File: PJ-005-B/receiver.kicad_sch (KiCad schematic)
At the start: 0 parts

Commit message: -- Transmitter with pre-amp LM7171 and power amp LT1210 -- Receiver with charge amp-->inverting amp-->4th order filter-->Inverting amp-->buffer -- Power with LDO 12V to 9V, 9V to 6V, 6V to 5V, 5V to 2.5V and -5V to -2.5V
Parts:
- added J3: Conn_01x02_Pin, symbol Connector:Conn_01x02_Pin
- added R50: 0R, symbol Device:R
- added U14: MD0105K6-G, symbol Echosounder Transceiver:MD0105K6-G
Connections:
- new net: J3.2 (Pin_2), U14.2 (A1)
- new net Charge Amp + Inverting Amp/AMP_OUT: R50.1
- new net Charge Amp + Inverting Amp/CHARGE_AMP_IN: U14.17 (B1)
- new net Filter + Inverting Amp + Buffer/FILTER_IN: R50.2
- new net GND: J3.1 (Pin_1), U14.19 (EPAD)
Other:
- added sheet Charge Amp + Inverting Amp (charge amp & inverting amp.kicad_sch)
- added sheet Filter + Inverting Amp + Buffer (filter & inverting amp & buffer.kicad_sch)
- added sheet PGA (pga.kicad_sch)
- company: (none) -> Xalten Systems Pvt. Ltd.
- title: (none) -> Echosounder Transceiver

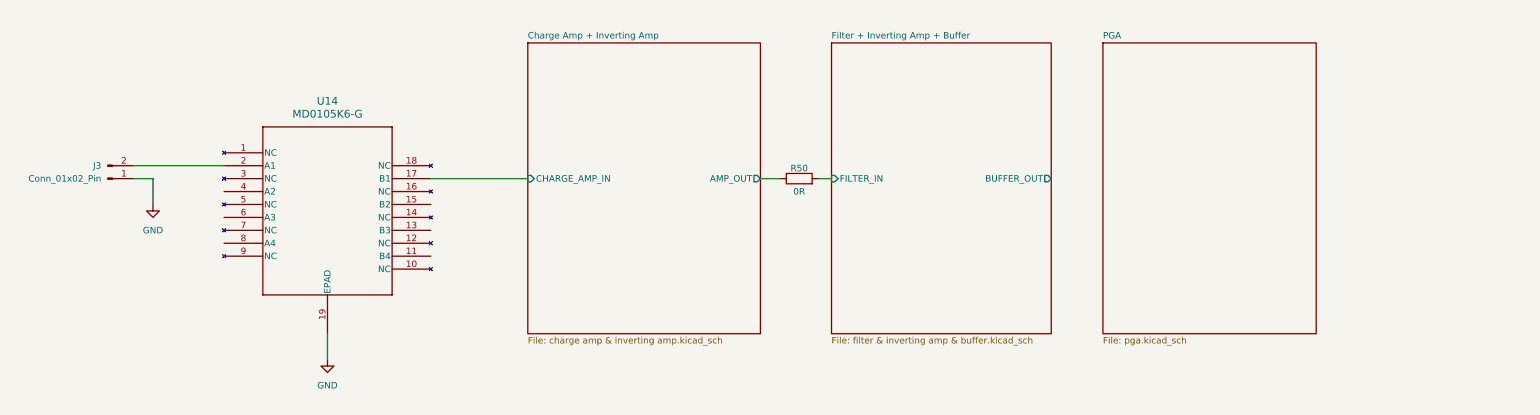
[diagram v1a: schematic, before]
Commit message: -- Receive stage with charge amp-->inverting amp-->BPF-->inverting amp-->buffer-->PGA-->buffer -- Transmit stage with push pull mosfet -- TTL to RS485 converter -- LDOs 12V to 9V, 9V to 6V, 6V to 5V, 5V to 2.5V and -5V to -2.5V
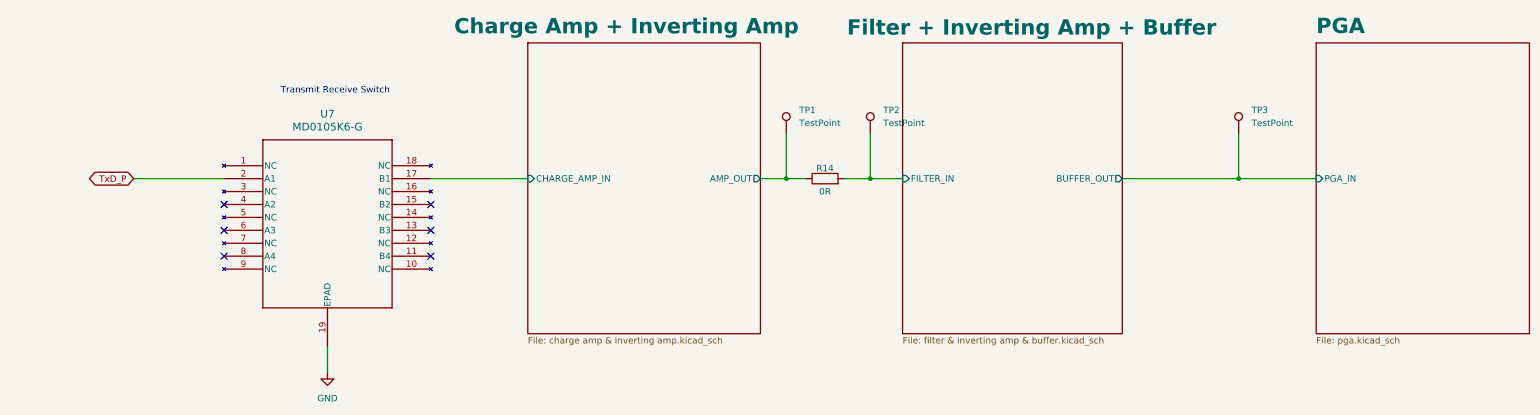
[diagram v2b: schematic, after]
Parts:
- removed J3: Conn_01x02_Pin, symbol Connector:Conn_01x02_Pin
- added TP1, TP2, TP3: TestPoint, TestPoint:TestPoint_Pad_1.0x1.0mm, symbol Connector:TestPoint
- R14: renamed from R50; footprint (none) -> XaltenFootprints:R0603
- U7: renamed from U14; footprint (none) -> Echosounder Transceiver FP:DFN18
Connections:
- net Charge Amp + Inverting Amp/AMP_OUT: now also TP1.1
- net Filter + Inverting Amp + Buffer/BUFFER_OUT: now also TP3.1
- net Filter + Inverting Amp + Buffer/FILTER_IN: now also TP2.1
- net TxD_P: now reaches U7.2 (A1)
- no-connect marks 0 -> 6
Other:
- sheet PGA ports: added PGA_IN; removed none
- note added: "Transmit Receive Switch"
- moved on the sheet: R14, U7

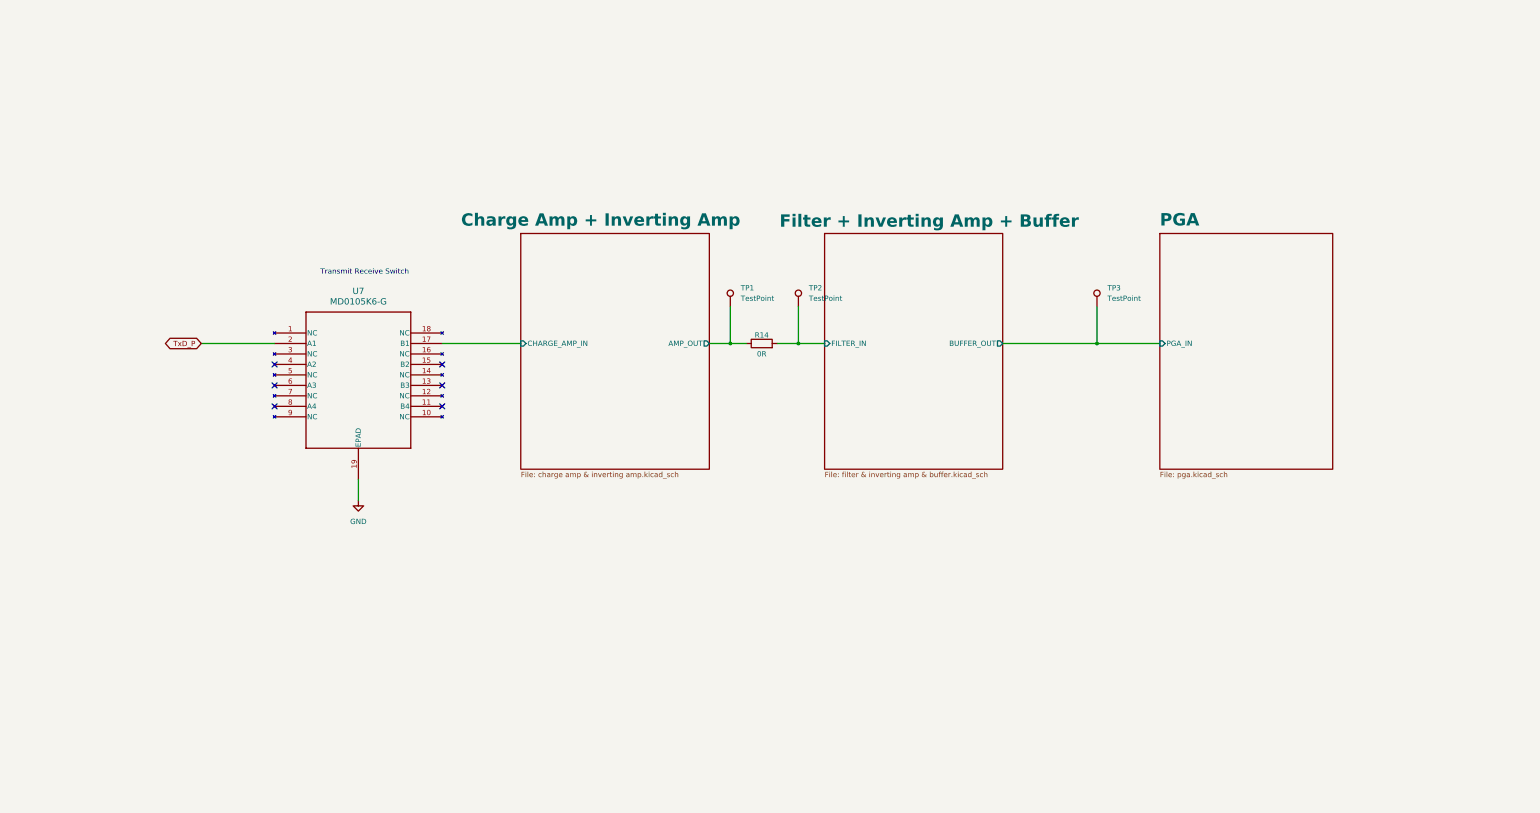
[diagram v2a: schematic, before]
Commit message: -- Reference Voltage IC removed -- Receiver includes only transmit receive switch and charge amp -- Changes in snubber values -- Changes in pull-up and pull-down resistors
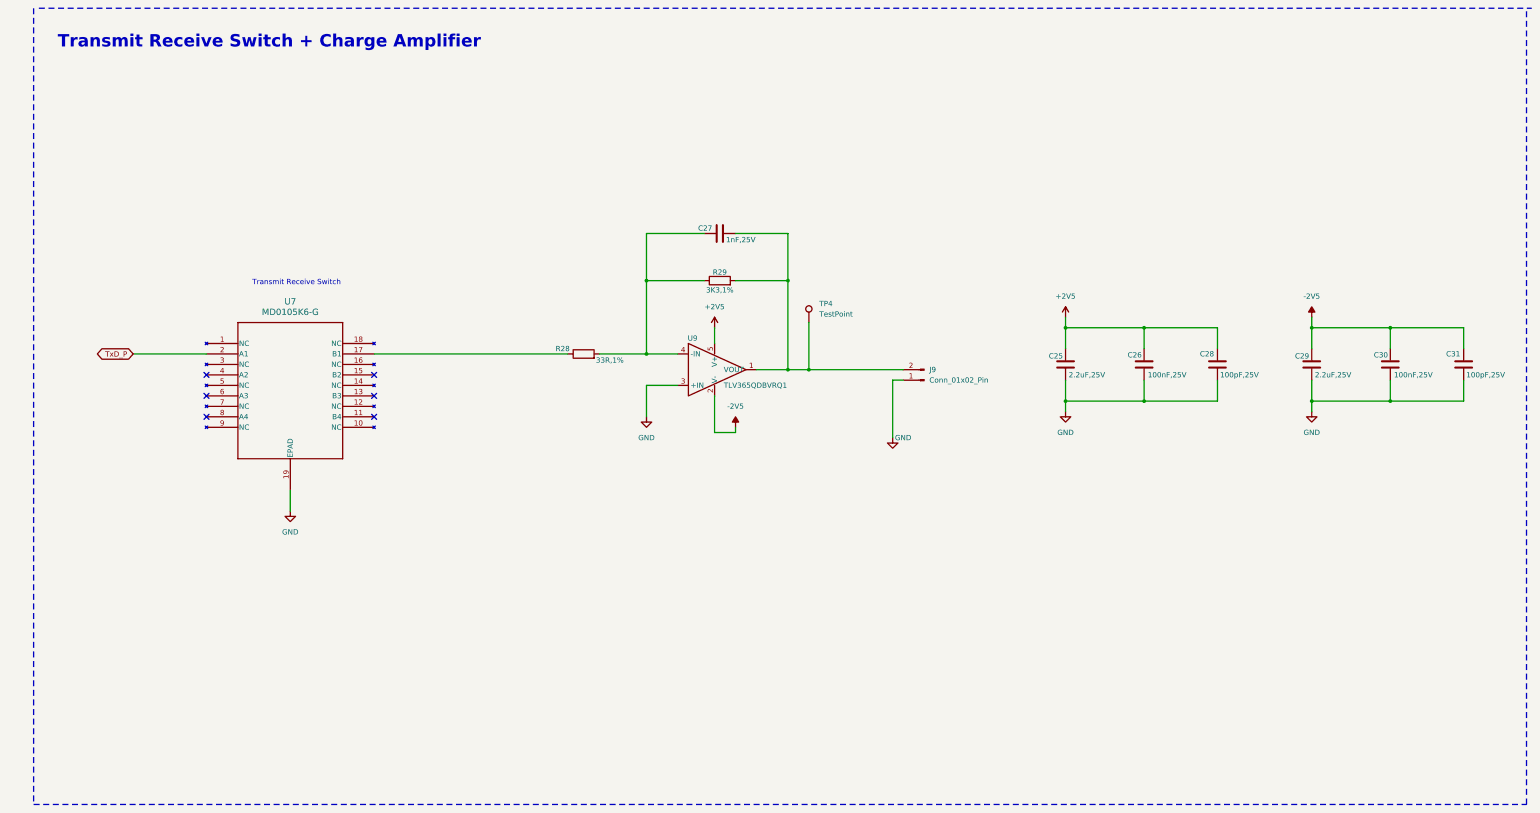
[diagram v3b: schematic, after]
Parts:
- removed R14: 0R, XaltenFootprints:R0603, symbol Device:R
- removed TP1, TP2, TP3: TestPoint, TestPoint:TestPoint_Pad_1.0x1.0mm, symbol Connector:TestPoint
- added C25, C29: 2.2uF,25V, XaltenFootprints:C0603, symbol Device:C
- added C26, C30: 100nF,25V, XaltenFootprints:C0603, symbol Device:C
- added C27: 1nF,25V, XaltenFootprints:C0603, symbol Device:C
- added C28, C31: 100pF,25V, XaltenFootprints:C0603, symbol Device:C
- added J9: Conn_01x02_Pin, Connector_PinHeader_2.54mm:PinHeader_1x02_P2.54mm_Vertical, symbol Connector:Conn_01x02_Pin
- added R28: 33R,1%, XaltenFootprints:R0603, symbol Device:R
- added R29: 3K3,1%, XaltenFootprints:R0603, symbol Device:R
- added TP4: TestPoint, TestPoint:TestPoint_Pad_1.0x1.0mm, symbol Connector:TestPoint
- added U9: TLV365QDBVRQ1, XaltenFootprints:SOT-23-5, symbol Echosounder Transceiver:TLV365QDBVRQ1
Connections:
- net GND: now also C25.2, C26.1, C28.1, C29.2, C30.1, C31.1, J9.1 (Pin_1), U9.3 (+IN)
- net Charge Amp + Inverting Amp/CHARGE_AMP_IN: no longer names the net of U7.17 (B1)
- net Charge Amp + Inverting Amp/CHARGE_AMP_IN: now also R28.1
- new net: C27.2, J9.2 (Pin_2), R29.2, TP4.1, U9.1 (VOUT)
- new net: C27.1, R28.2, R29.1, U9.4 (-IN)
- new net +2V5: C25.1, C26.2, C28.2, U9.5 (V+)
- new net -2V5: C29.1, C30.2, C31.2, U9.2 (V-)
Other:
- removed sheet Charge Amp + Inverting Amp
- removed sheet Filter + Inverting Amp + Buffer
- removed sheet PGA
- note added: "Transmit Receive Switch + Charge Amplifier"
- moved on the sheet: U7
